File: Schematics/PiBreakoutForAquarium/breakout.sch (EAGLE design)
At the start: 17 parts, among them U1 MSP430G2402IN20

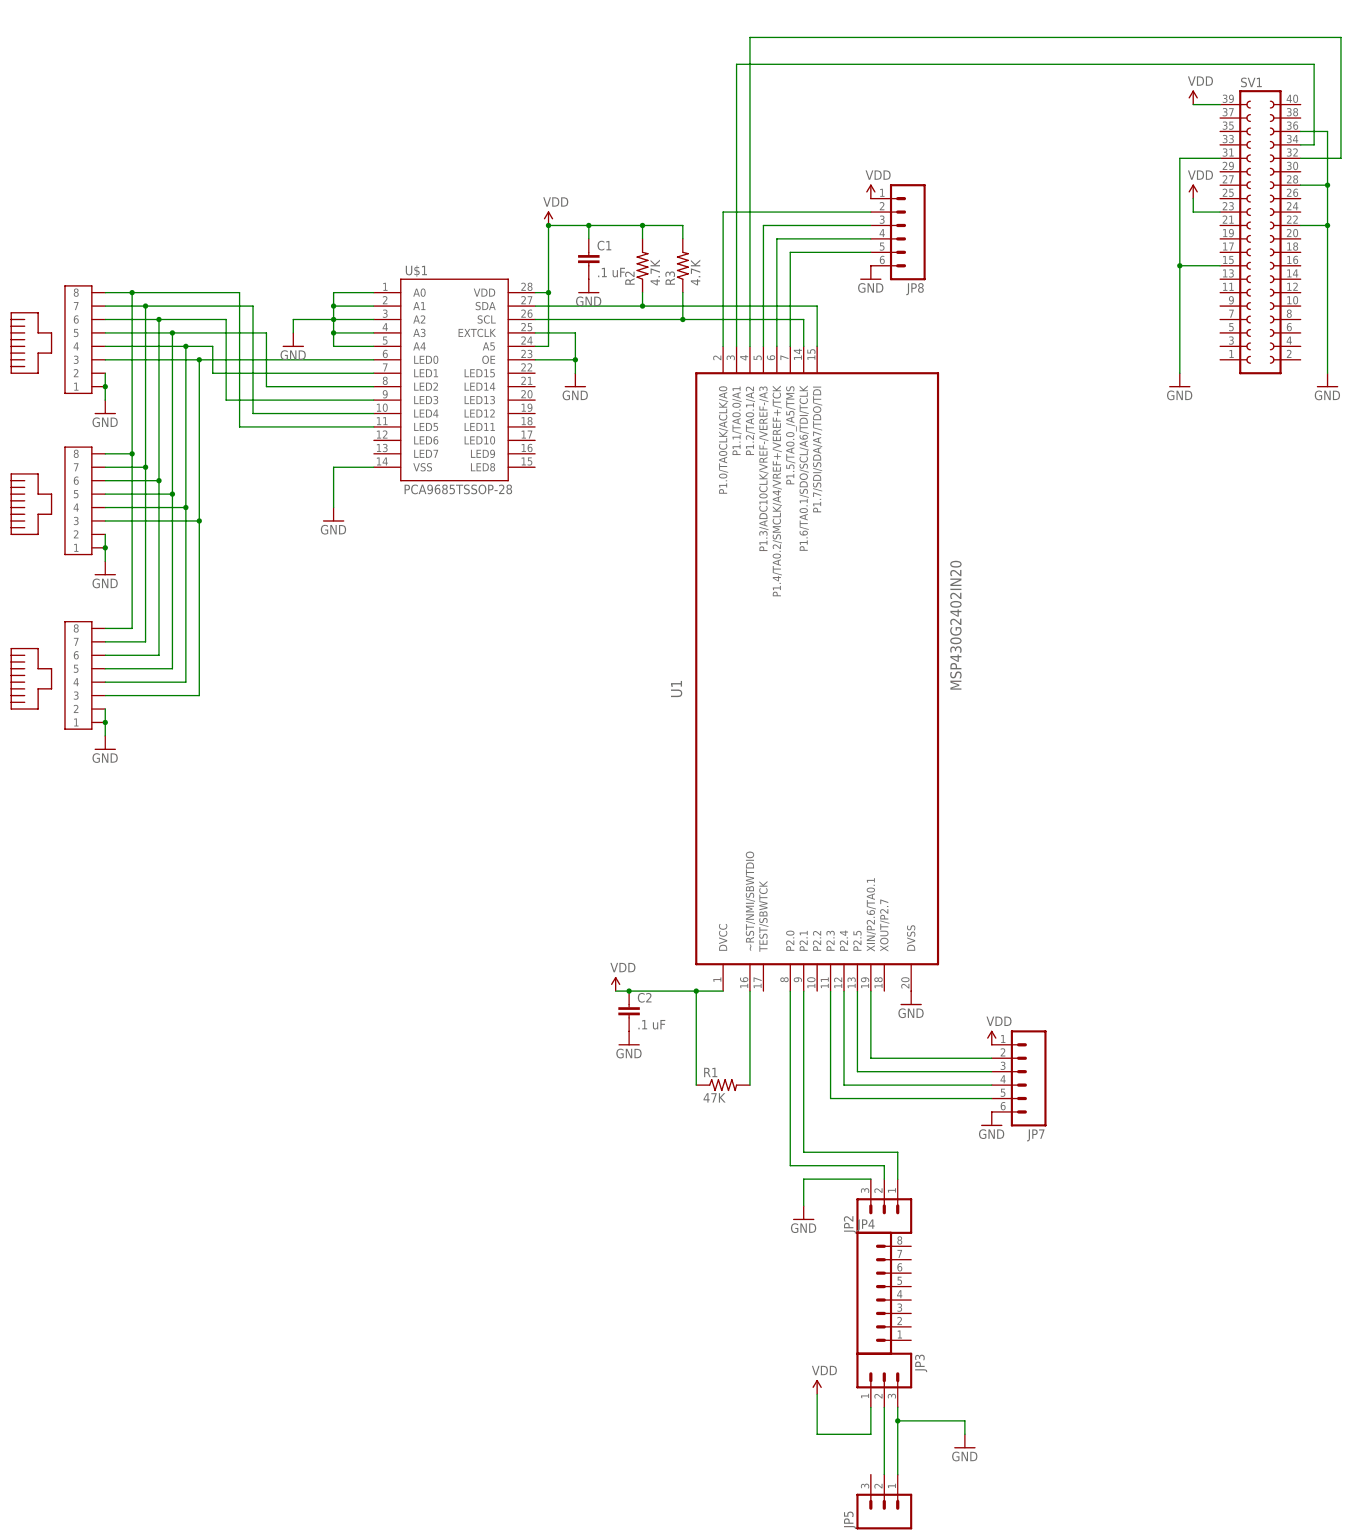
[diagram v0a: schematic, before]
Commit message: New AVR based firmware
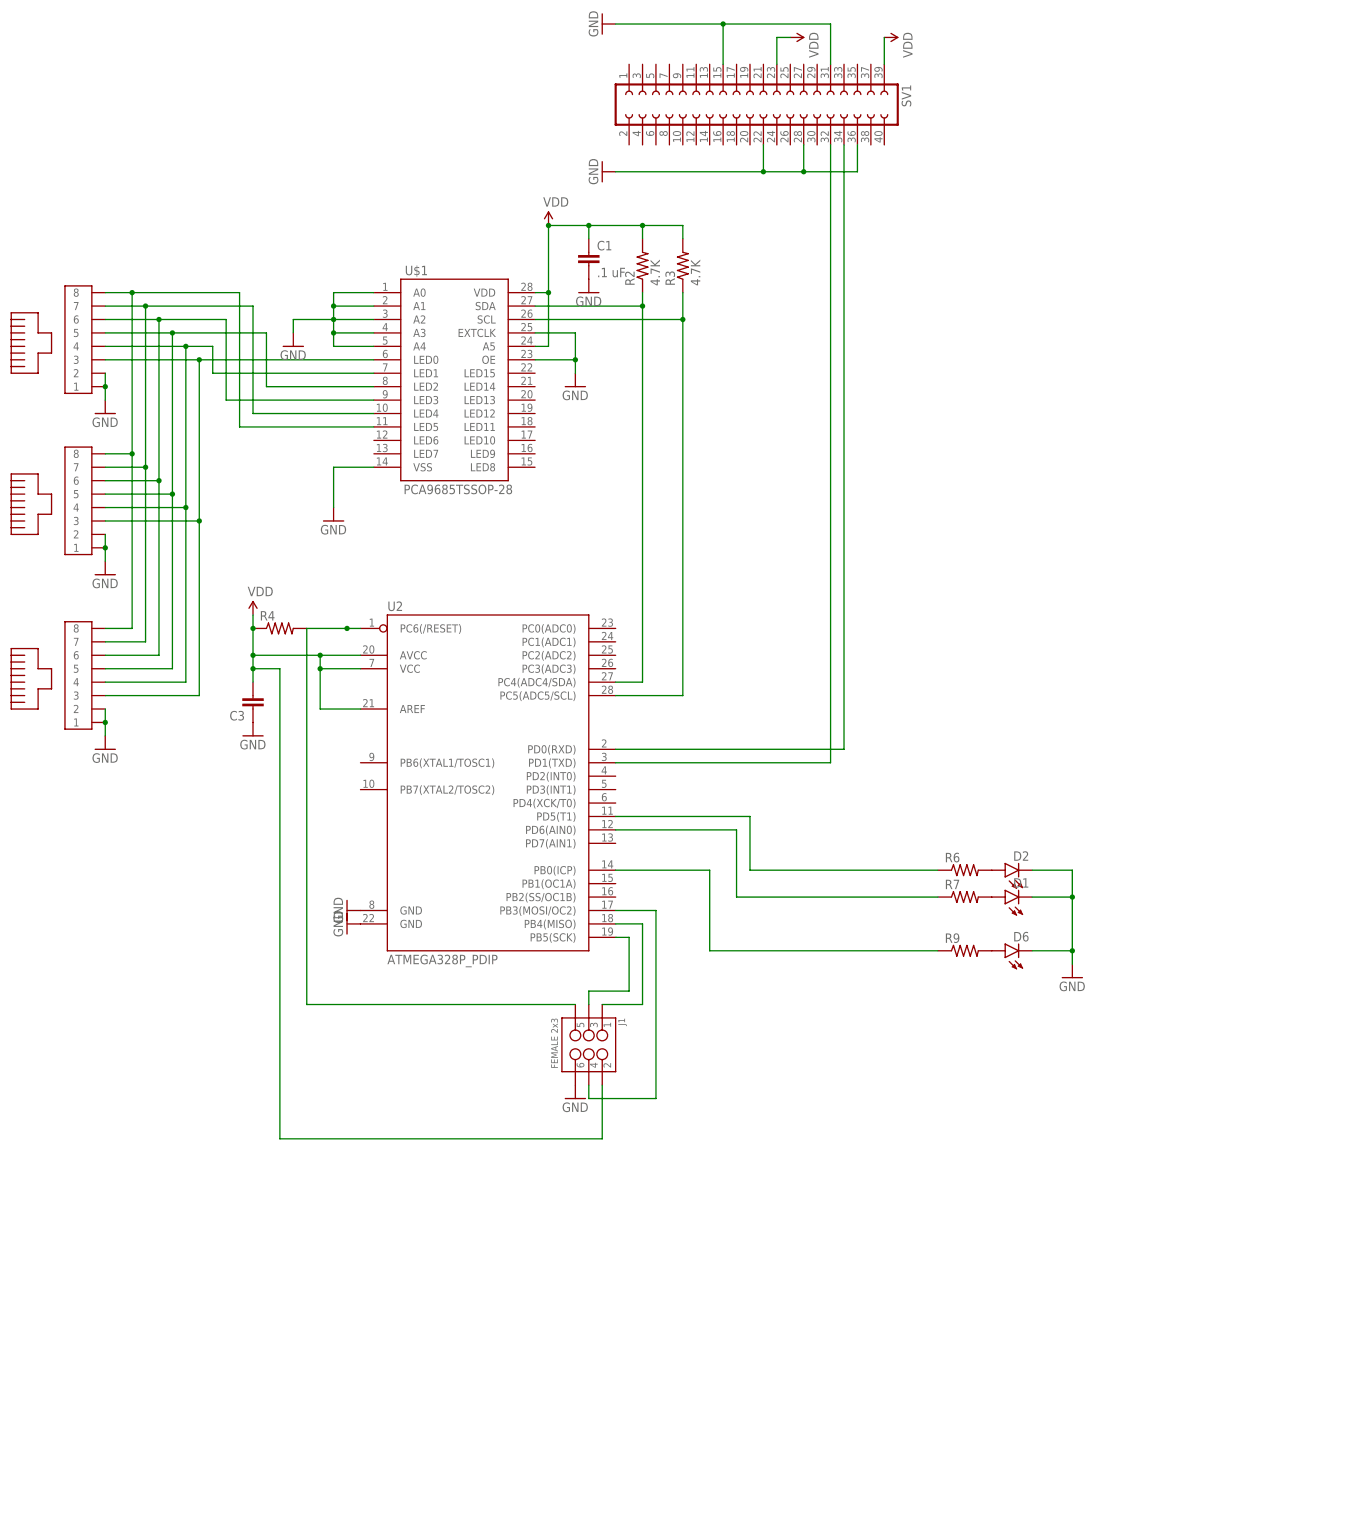
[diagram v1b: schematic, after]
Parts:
- removed C2: .1 uF, SparkFun-Capacitors:CAP1206
- removed JP2, JP3, JP5: (no value), SparkFun-Connectors:M03PTH
- removed JP4: (no value), SparkFun-Connectors:M081X08
- removed JP7, JP8: (no value), SparkFun-Connectors:M06LONGPADS
- removed R1: 47K, SparkFun-Resistors:RESISTOR1206
- removed U1: MSP430G2402IN20, Texas Instruments_By_element14_Batch_1:MSP430G2402IN20
- added C3: (no value), SparkFun-Capacitors:CAP1206
- added D1, D2, D6: (no value), SparkFun-LED:LED0603
- added J1: FEMALE 2x3, SparkFun-Connectors:M03X2FEMALE
- added R4, R6, R7, R9: (no value), SparkFun-Resistors:RESISTOR1206
- added U2: ATMEGA328P_PDIP, SparkFun-DigitalIC:ATMEGA328P_PDIP
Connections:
- removed net N$19: JP7.3, U1.P2.5
- removed net N$22: JP8.3, U1.P1.3/ADC10CLK/VREF-/VEREF-/A3
- removed net N$5: R3.1, U$1.SCL, U1.P1.6/TA0.1/SDO/SCL/A6/TDI/TCLK
- removed net N$6: R1.2, U1.~RST/NMI/SBWTDIO
- new net N$16: J1.1, U2.PB4(MISO)
- new net N$25: R3.1, U$1.SCL, U2.PC5(ADC5/SCL)
- net GND: now also C3.1, D1.C, D2.C, D6.C, J1.6, U2.GND@1, U2.GND@2; no longer C2.2, JP2.3, JP3.3, JP5.1, JP7.6, JP8.6, U1.DVSS
- net N$1: now also U2.PD1(TXD); no longer U1.P1.2/TA0.1/A2
- net N$10: now also U2.PD0(RXD); no longer U1.P1.1/TA0.0/A1
- net N$17: now also J1.3, U2.PB5(SCK); no longer JP7.5, U1.P2.3
- net N$18: now also D1.A, R7.2; no longer JP7.4, U1.P2.4
- net N$2: now also J1.5, R4.2, U2.PC6(/RESET); no longer JP2.1, U1.P2.1
- net N$20: now also D6.A, R9.2; no longer JP7.2, U1.XIN/P2.6/TA0.1
- net N$21: now also R9.1, U2.PB0(ICP); no longer JP8.2, U1.P1.0/TA0CLK/ACLK/A0
- net N$23: now also R7.1, U2.PD6(AIN0); no longer JP8.4, U1.P1.4/TA0.2/SMCLK/A4/VREF+/VEREF+/TCK
- net N$24: now also R6.1, U2.PD5(T1); no longer JP8.5, U1.P1.5/TA0.0_/A5/TMS
- net N$4: now also U2.PC4(ADC4/SDA); no longer U1.P1.7/SDI/SDA/A7/TDO/TDI
- net N$7: now also D2.A, R6.2; no longer JP3.2, JP5.2
- net N$8: now also J1.4, U2.PB3(MOSI/OC2); no longer JP2.2, U1.P2.0
- net VDD: now also C3.2, J1.2, R4.1, U2.AREF, U2.AVCC, U2.VCC; no longer C2.1, JP3.1, JP7.1, JP8.1, R1.1, U1.DVCC
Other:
- moved on the sheet: SV1
